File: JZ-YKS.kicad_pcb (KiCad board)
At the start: 2 copper layers, 50 x 50 mm, 0 parts

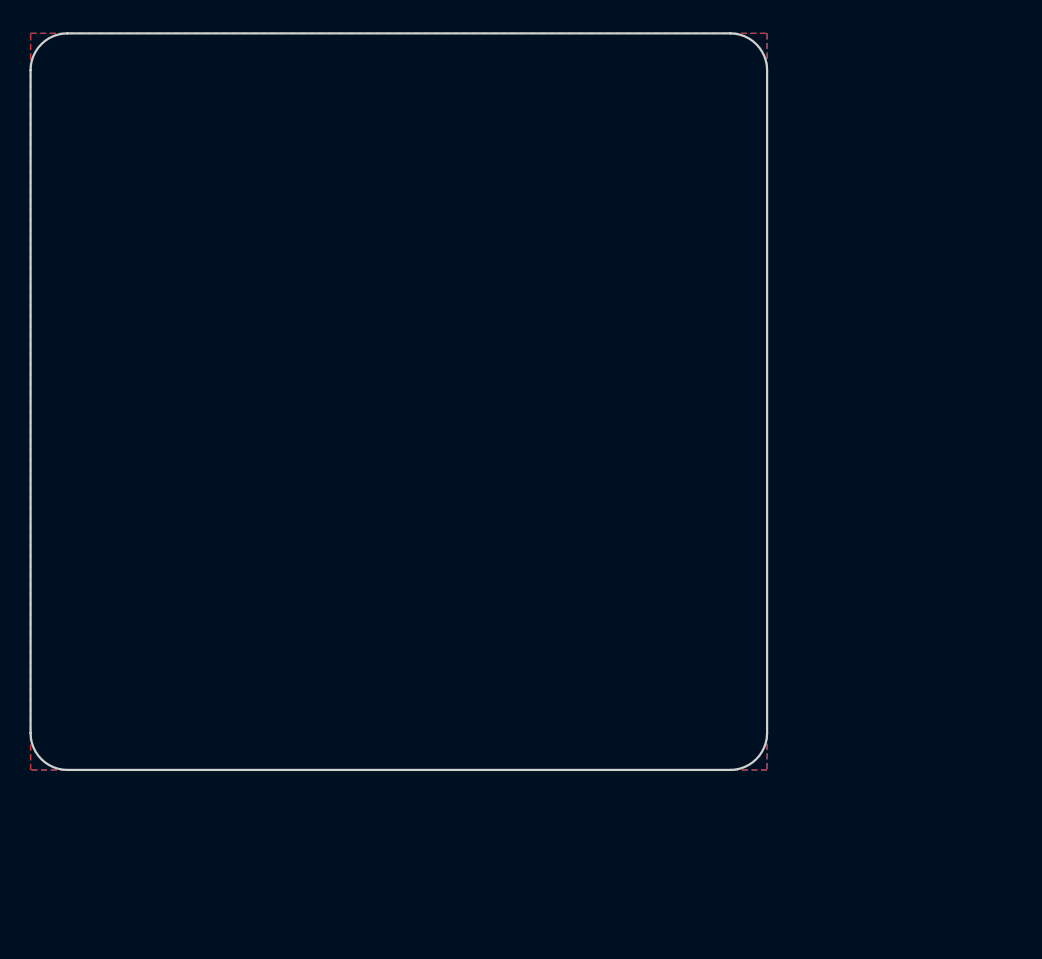
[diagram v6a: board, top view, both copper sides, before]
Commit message: RAM and NAND successfully routed
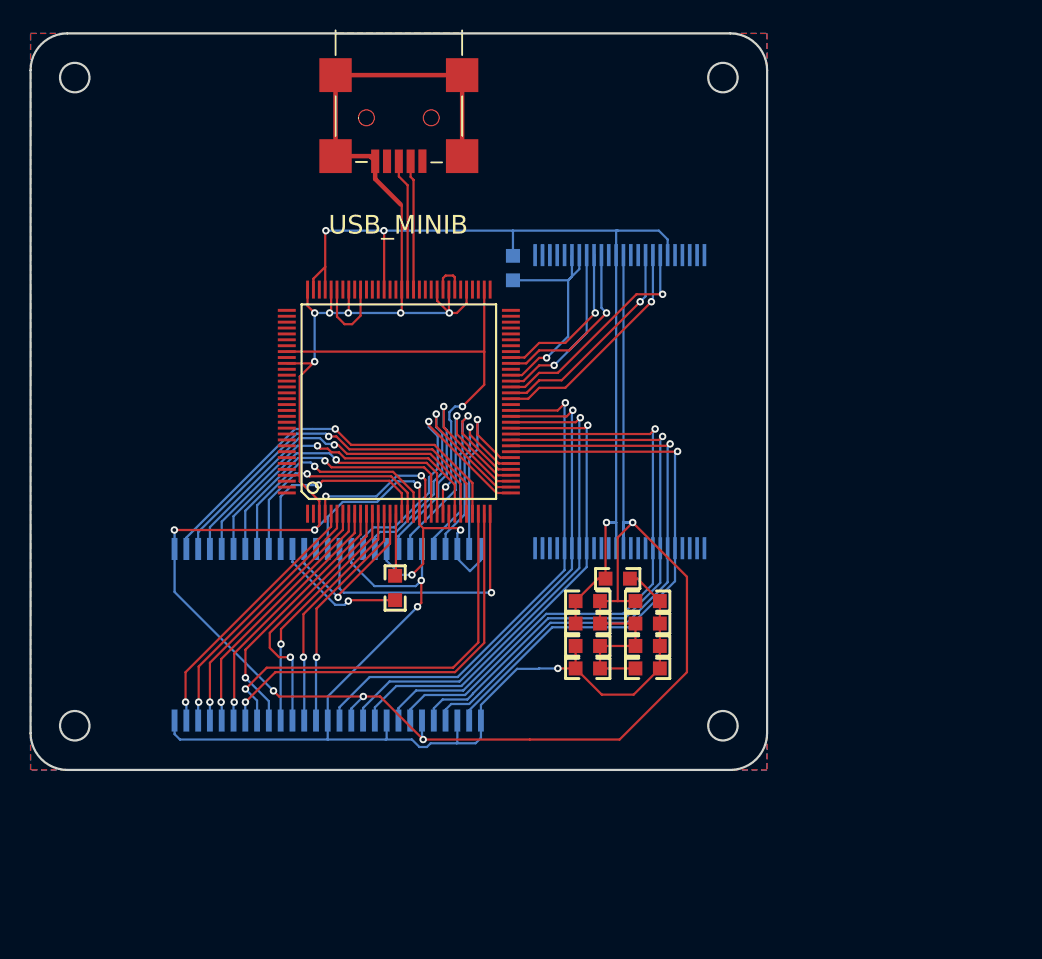
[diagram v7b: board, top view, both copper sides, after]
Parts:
- added C21: 0.1uF, size-0603, F.Cu at (151.9, 113.5)
- added C22: 0.1uF, size-0603, F.Cu at (151.9, 115.1)
- added C23: 0.1uF, size-0603, F.Cu at (151.9, 116.6)
- added C24: 0.1uF, size-0603, F.Cu at (151.9, 118.1)
- added C25: 0.1uF, size-0603, F.Cu at (147.8, 118.1)
- added C26: 10uF, size-0603, F.Cu at (147.8, 116.6)
- added C27: 0.1uF, size-0603, F.Cu at (147.8, 115.1)
- added C28: 10uF, size-0603, F.Cu at (147.8, 113.5)
- added FB9: BKP1608HS121, size-0603, F.Cu at (149.9, 112.0)
- added IC1: JZ4725, JZ-LQFP128, F.Cu at (135.0, 100.0)
- added J1: USB_MINIB, CON_USB_MB, F.Cu at (135.0, 75.0)
- added R6: 33, size-0603, F.Cu at (134.7, 112.6)
- added R7: 100k, size-0603, B.Cu at (142.7, 90.9)
- added U4: HY27UG088G5M, tsop48, B.Cu at (150.0, 100.0)
- added U5: P3V56S40ETP-G6, tsop54, B.Cu at (130.2, 115.8)
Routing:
- net GND: track 0.00 -> 213.5 mm, vias 0 -> 15
- net N-00000159: track 0.00 -> 73.0 mm, vias 0 -> 3
- net +3.3V: track 0.00 -> 69.0 mm, vias 0 -> 3
- net D3: track 0.00 -> 41.3 mm, vias 0 -> 1
- net D2: track 0.00 -> 40.2 mm, vias 0 -> 1
- net D1: track 0.00 -> 39.7 mm, vias 0 -> 1
- net D0: track 0.00 -> 38.5 mm, vias 0 -> 1
- net D7: track 0.00 -> 35.3 mm, vias 0 -> 1
- net D6: track 0.00 -> 34.1 mm, vias 0 -> 1
- net D5: track 0.00 -> 33.8 mm, vias 0 -> 1
- net D4: track 0.00 -> 32.6 mm, vias 0 -> 1
- net N-00000101: track 0.00 -> 30.2 mm, vias 0 -> 2
- net A13: track 0.00 -> 28.3 mm, vias 0 -> 1
- net A14: track 0.00 -> 27.9 mm, vias 0 -> 1
- net A4: track 0.00 -> 26.9 mm, vias 0 -> 1
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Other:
- outline, holes or cut-outs redrawn

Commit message: far from ideal, but still ready for production
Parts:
- added C1: 0.1uF, size-0603, B.Cu at (135.8, 95.1)
- added C10: 1uF, size-0603, B.Cu at (137.1, 91.9)
- added C11: 0.01uF, size-0603, B.Cu at (126.9, 92.5)
- added C12: 0.01uF, size-0603, B.Cu at (131.4, 97.0)
- added C13: 0.1uF, size-0603, B.Cu at (131.4, 98.6)
- added C14: 10uF, size-0603, B.Cu at (131.4, 100.1)
- added C15: 10uF, size-0603, B.Cu at (126.9, 94.0)
- added C16: 22pF, size-0603, F.Cu at (138.0, 88.0)
- added C17: 22pF, size-0603, F.Cu at (125.5, 89.7)
- added C18: 22pF, size-0603, F.Cu at (128.4, 83.6)
- added C19: 22pF, size-0603, F.Cu at (144.5, 88.1)
- added C2: 10uF, size-0603, B.Cu at (139.1, 95.1)
- added C29: 1uF, size-0603, B.Cu at (135.0, 86.2)
- added C3: 0.1uF, size-0603, B.Cu at (139.1, 96.6)
- added C30: 1uF, size-0603, B.Cu at (144.4, 85.7)
- added C31: 1uF, size-0603, B.Cu at (142.7, 87.8)
- added C4: 0.1uF, size-0603, B.Cu at (139.1, 98.2)
- added C5: 0.1uF, size-0603, B.Cu at (132.3, 103.5)
- added C6: 10uF, size-0603, B.Cu at (133.9, 103.5)
- added C7: 1uF, size-0603, B.Cu at (137.1, 90.4)
- added C8: 1uF, size-0603, B.Cu at (131.8, 95.1)
- added C9: 0.1uF, size-0603, B.Cu at (135.9, 98.2)
- added FB1: BKP1608HS121, size-0603, B.Cu at (141.0, 89.4)
- added FB2: BKP1608HS121, size-0603, B.Cu at (135.8, 101.5)
- added FB3: BKP1608HS121, size-0603, B.Cu at (134.7, 96.6)
- added FB5: BKP1608HS121, size-0603, B.Cu at (133.9, 92.3)
- added FB6: BKP1608HS121, size-0603, B.Cu at (126.9, 95.5)
- added FB7: BKP1608HS121, size-0603, B.Cu at (134.0, 100.3)
- added G***: LOGO, OSHWLOGO0.75IN, F.Cu at (125.0, 107.0)
- added R1: 10k, size-0603, B.Cu at (137.1, 93.3)
- added R2: 33, size-0603, F.Cu at (132.1, 88.8)
- added R3: 33, size-0603, F.Cu at (140.5, 88.0)
- added R4: 10M, size-0603, F.Cu at (128.0, 88.8)
- added R5: 1M, size-0603, F.Cu at (143.5, 91.8)
- added U1: PINHEAD30, pinhead-double-2.54mm-30, F.Cu at (115.0, 100.0)
- added U10: PINHEAD2, pinhead-1.27mm-2, F.Cu at (155.5, 113.0)
- added U2: PINHEAD8, pinhead-double-1.27mm-8, F.Cu at (122.0, 84.0)
- added U3: VREG-DUAL, sot23-6, B.Cu at (139.2, 86.4)
- added U6: PINHEAD6, pinhead-1.27mm-6, F.Cu at (155.0, 84.5)
- added U7: PINHEAD4, pinhead-1.27mm-4, F.Cu at (149.0, 87.0)
- added U8: PINHEAD3, pinhead-2.54mm-3, F.Cu at (148.0, 79.0)
- added U9: PINHEAD8, pinhead-double-1.27mm-8, F.Cu at (122.0, 79.0)
- added X1: , crystal, F.Cu at (132.2, 86.7)
- added X2: , crystal, F.Cu at (142.5, 89.2)
- J1: value USB_MINIB -> (none)
- R6: moved to B.Cu
- moved R6 8.08 mm to (128.9, 107.1), turned to 0 degrees
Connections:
- net N-00000101 renamed /VDDIO
- net N-00000102 renamed /VDDCORE
- net N-00000159 renamed /memory/MEM_VCC
- IC1 pad 100: N-0000099 -> BOOT_1
- IC1 pad 101: N-00000100 -> BOOT_0
- IC1 pad 84: N-00000105 -> PPRST
- IC1 pad 85: N-00000103 (its old number) -> WKUP
- IC1 pad 86: N-00000104 (its old number) -> PWRON
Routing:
- net GND: track 213.5 -> 339.0 mm, vias 15 -> 17
- net +3.3V: track 69.0 -> 173.6 mm, vias 3 -> 6
- net SD_CD: track 0.00 -> 28.8 mm
- net SD_DO: track 0.00 -> 26.0 mm, vias 0 -> 2
- net RXD: track 0.00 -> 25.7 mm
- net TXD: track 0.00 -> 25.7 mm
- net +1.8V: track 0.00 -> 25.3 mm
- net ADIN1: track 0.00 -> 24.7 mm, vias 0 -> 2
- net WKUP: track 0.00 -> 24.3 mm
- net ADIN0: track 0.00 -> 24.2 mm, vias 0 -> 2
- net SD_CLK: track 0.00 -> 23.7 mm, vias 0 -> 2
- net PWM: track 0.00 -> 23.3 mm
- net PWRON: track 0.00 -> 22.2 mm
- net HP_R: track 0.00 -> 21.9 mm, vias 0 -> 1
- net SD_CMD: track 0.00 -> 21.3 mm, vias 0 -> 2
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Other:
- outline, holes or cut-outs redrawn
- board text added: "AUDIO"
- board text added: "I²C"
- board text added: "JZ-YKS (rev A) CYB3R 2014"
- board text added: "JZ4725B"
- board text added: "NAND FLASH"
- board text added: "POWER"
- board text added: "PWM"
- board text added: "RAM"
- board text added: "SD"
- board text added: "UART"
